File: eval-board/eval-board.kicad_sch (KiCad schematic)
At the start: 0 parts

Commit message: eval top level
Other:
- added sheet Barometer (baro.kicad_sch)
- added sheet FCU (fcu.kicad_sch)
- added sheet IMU0 (imu0.kicad_sch)
- added sheet IMU1 (imu1.kicad_sch)
- added sheet Magnetometer (mag.kicad_sch)
- added sheet PMU (pmu.kicad_sch)
- added sheet WCU (wcu.kicad_sch)

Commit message: pmu schematic
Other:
- sheet PMU ports: added +3V3A, +3V3D, +3V3D_PG, +5V, VIN; removed none
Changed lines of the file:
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@@
 	)
 	(sheet
-		(at 30.48 88.9)
-		(size 40.64 38.1)
+		(at 35.56 92.71)
+		(size 17.78 12.7)
 		(exclude_from_sim no)
 		(in_bom yes)
@@
 		)
 		(property "Sheetname" "PMU"
-			(at 30.48 88.1884 0)
+			(at 35.56 91.9984 0)
 			(show_name no)
 			(do_not_autoplace no)
@@
 		)
 		(property "Sheetfile" "pmu.kicad_sch"
-			(at 30.48 127.5846 0)
+			(at 35.56 105.9946 0)
 			(show_name no)
 			(do_not_autoplace no)
@@
 			)
 		)
+		(pin "VIN" input
+			(at 35.56 95.25 180)
+			(effects
+				(font
+					(size 1.27 1.27)
+				)
+				(justify left)
+			)
+		)
+		(pin "+5V" output
+			(at 53.34 95.25 0)
+			(effects
+				(font
+					(size 1.27 1.27)
+				)
+				(justify right)
+			)
+		)
+		(pin "+3V3A" output
+			(at 53.34 97.79 0)
+			(effects
+				(font
+					(size 1.27 1.27)
+				)
+				(justify right)
+			)
+		)
+		(pin "+3V3D_PG" output
+			(at 53.34 102.87 0)
+			(effects
+				(font
+					(size 1.27 1.27)
+				)
+				(justify right)
+			)
+		)
+		(pin "+3V3D" output
+			(at 53.34 100.33 0)
+			(effects
+				(font
+					(size 1.27 1.27)
+				)
+				(justify right)
+			)
+		)

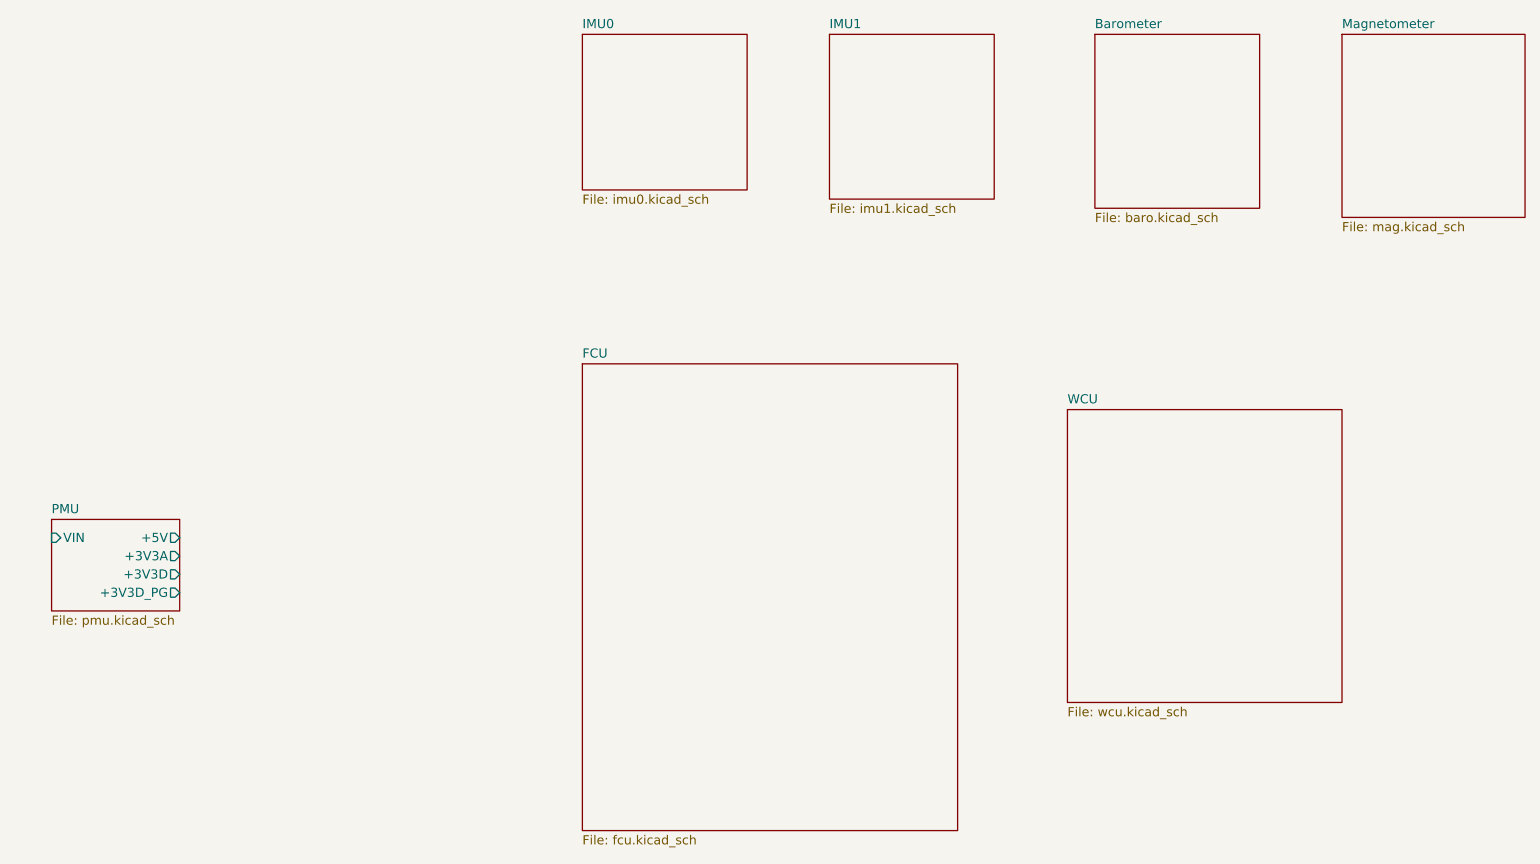
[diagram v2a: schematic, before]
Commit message: imu0 - lsm6dso
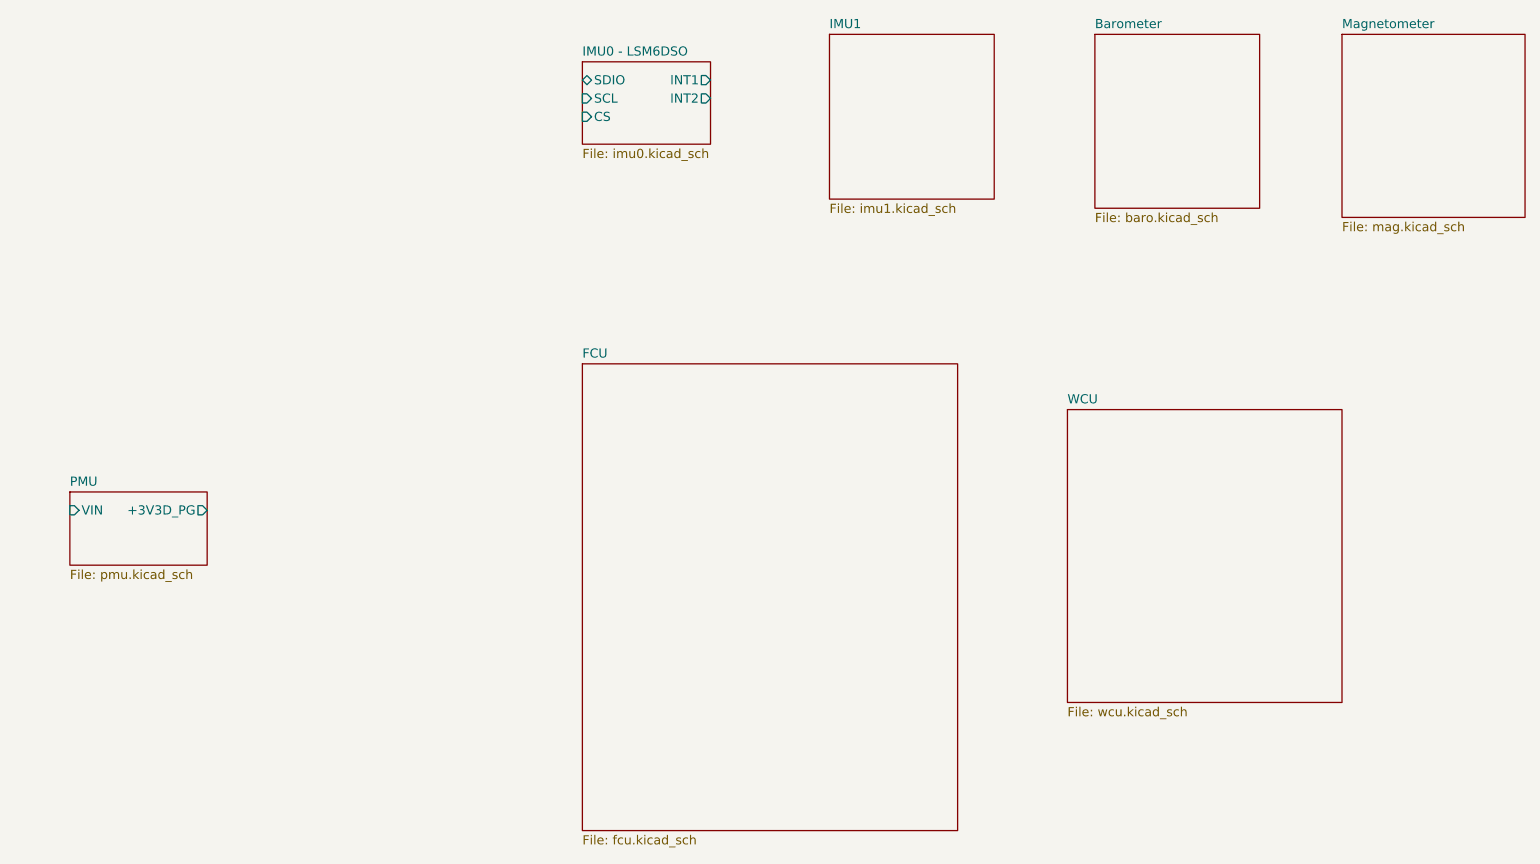
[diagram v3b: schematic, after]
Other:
- sheet IMU0 renamed IMU0 - LSM6DSO
- sheet IMU0 - LSM6DSO ports: added CS, INT1, INT2, SCL, SDIO; removed none
- sheet PMU ports: added none; removed +3V3A, +3V3D, +5V
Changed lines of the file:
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@@
 	)
 	(sheet
-		(at 109.22 25.4)
-		(size 22.86 21.59)
+		(at 109.22 29.21)
+		(size 17.78 11.43)
 		(exclude_from_sim no)
 		(in_bom yes)
@@
 			(color 0 0 0 0)
 		)
-		(property "Sheetname" "IMU0"
-			(at 109.22 24.6884 0)
+		(property "Sheetname" "IMU0 - LSM6DSO"
+			(at 109.22 28.4984 0)
 			(show_name no)
 			(do_not_autoplace no)
@@
 		)
 		(property "Sheetfile" "imu0.kicad_sch"
-			(at 109.22 47.5746 0)
+			(at 109.22 41.2246 0)
 			(show_name no)
 			(do_not_autoplace no)
@@
 				)
 				(justify left top)
+			)
+		)
+		(pin "SDIO" bidirectional
+			(at 109.22 31.75 180)
+			(effects
+				(font
+					(size 1.27 1.27)
+				)
+				(justify left)
+			)
+		)
+		(pin "SCL" input
+			(at 109.22 34.29 180)
+			(effects
+				(font
+					(size 1.27 1.27)
+				)
+				(justify left)
+			)
+		)
+		(pin "CS" input
+			(at 109.22 36.83 180)
+			(effects
+				(font
+					(size 1.27 1.27)
+				)
+				(justify left)
+			)
+		)
+		(pin "INT2" output
+			(at 127 34.29 0)
+			(effects
+				(font
+					(size 1.27 1.27)
+				)
+				(justify right)
+			)
+		)
+		(pin "INT1" output
+			(at 127 31.75 0)
+			(effects
+				(font
+					(size 1.27 1.27)
+				)
+				(justify right)
 			)
 		)
@@
 	)
 	(sheet
-		(at 35.56 92.71)
-		(size 17.78 12.7)
+		(at 38.1 88.9)
+		(size 19.05 10.16)
 		(exclude_from_sim no)
 		(in_bom yes)
@@
 		)
 		(property "Sheetname" "PMU"
-			(at 35.56 91.9984 0)
+			(at 38.1 88.1884 0)
 			(show_name no)
 			(do_not_autoplace no)
@@
 		)
 		(property "Sheetfile" "pmu.kicad_sch"
-			(at 35.56 105.9946 0)
+			(at 38.1 99.6446 0)
 			(show_name no)
 			(do_not_autoplace no)
@@
 		)
 		(pin "VIN" input
-			(at 35.56 95.25 180)
+			(at 38.1 91.44 180)
 			(effects
 				(font
@@
 			)
 		)
-		(pin "+5V" output
-			(at 53.34 95.25 0)
+		(pin "+3V3D_PG" output
+			(at 57.15 91.44 0)
 			(effects
 				(font
-					(size 1.27 1.27)
-				)
-				(justify right)
-			)
-		)
-		(pin "+3V3A" output
-			(at 53.34 97.79 0)
-			(effects
-				(font
-					(size 1.27 1.27)
-				)
-				(justify right)
-			)
-		)
-		(pin "+3V3D_PG" output
-			(at 53.34 102.87 0)
-			(effects
-				(font
-					(size 1.27 1.27)
-				)
-				(justify right)
-			)
-		)
-		(pin "+3V3D" output
-			(at 53.34 100.33 0)
-			(effects
-				(font

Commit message: imu1, baro, mag
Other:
- sheet Barometer renamed Barometer - BMP388
- sheet IMU1 renamed IMU1 - BMI270
- sheet Barometer - BMP388 ports: added INT, SCL, SDA; removed none
- sheet IMU0 - LSM6DSO ports: added SCLK; removed SCL
- sheet IMU1 - BMI270 ports: added CS, INT1, INT2, SCLK, SDIO; removed none
- sheet Magnetometer ports: added SCL, SDA; removed none
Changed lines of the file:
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@@
 	(paper "A4")
 	(sheet
-		(at 143.51 25.4)
-		(size 22.86 22.86)
-		(exclude_from_sim no)
-		(in_bom yes)
-		(on_board yes)
-		(dnp no)
-		(fields_autoplaced yes)
-		(stroke
-			(width 0.1524)
-			(type solid)
-		)
-		(fill
-			(color 0 0 0 0)
-		)
-		(property "Sheetname" "IMU1"
-			(at 143.51 24.6884 0)
+		(at 69.85 38.1)
+		(size 20.32 11.43)
+		(exclude_from_sim no)
+		(in_bom yes)
+		(on_board yes)
+		(dnp no)
+		(fields_autoplaced yes)
+		(stroke
+			(width 0.1524)
+			(type solid)
+		)
+		(fill
+			(color 0 0 0 0)
+		)
+		(property "Sheetname" "IMU1 - BMI270"
+			(at 69.85 37.3884 0)
 			(show_name no)
 			(do_not_autoplace no)
@@
 		)
 		(property "Sheetfile" "imu1.kicad_sch"
-			(at 143.51 48.8446 0)
-			(show_name no)
-			(do_not_autoplace no)
-			(effects
-				(font
-					(size 1.27 1.27)
-				)
-				(justify left top)
+			(at 69.85 50.1146 0)
+			(show_name no)
+			(do_not_autoplace no)
+			(effects
+				(font
+					(size 1.27 1.27)
+				)
+				(justify left top)
+			)
+		)
+		(pin "INT1" output
+			(at 90.17 40.64 0)
+			(effects
+				(font
+					(size 1.27 1.27)
+				)
+				(justify right)
+			)
+		)
+		(pin "INT2" output
+			(at 90.17 43.18 0)
+			(effects
+				(font
+					(size 1.27 1.27)
+				)
+				(justify right)
+			)
+		)
+		(pin "SDIO" bidirectional
+			(at 69.85 40.64 180)
+			(effects
+				(font
+					(size 1.27 1.27)
+				)
+				(justify left)
+			)
+		)
+		(pin "CS" input
+			(at 69.85 45.72 180)
+			(effects
+				(font
+					(size 1.27 1.27)
+				)
+				(justify left)
+			)
+		)
+		(pin "SCLK" input
+			(at 69.85 43.18 180)
+			(effects
+				(font
+					(size 1.27 1.27)
+				)
+				(justify left)
 			)
 		)
@@
 	)
 	(sheet
-		(at 214.63 25.4)
-		(size 25.4 25.4)
+		(at 132.08 38.1)
+		(size 12.7 11.43)
 		(exclude_from_sim no)
 		(in_bom yes)
@@
 		)
 		(property "Sheetname" "Magnetometer"
-			(at 214.63 24.6884 0)
+			(at 132.08 37.3884 0)
 			(show_name no)
 			(do_not_autoplace no)
@@
 		)
 		(property "Sheetfile" "mag.kicad_sch"
-			(at 214.63 51.3846 0)
-			(show_name no)
-			(do_not_autoplace no)
-			(effects
-				(font
-					(size 1.27 1.27)
-				)
-				(justify left top)
+			(at 132.08 50.1146 0)
+			(show_name no)
+			(do_not_autoplace no)
+			(effects
+				(font
+					(size 1.27 1.27)
+				)
+				(justify left top)
+			)
+		)
+		(pin "SDA" bidirectional
+			(at 132.08 40.64 180)
+			(effects
+				(font
+					(size 1.27 1.27)
+				)
+				(justify left)
+			)
+		)
+		(pin "SCL" input
+			(at 132.08 43.18 180)
+			(effects
+				(font
+					(size 1.27 1.27)
+				)
+				(justify left)
 			)
 		)
@@
 	)
 	(sheet
-		(at 180.34 25.4)
-		(size 22.86 24.13)
-		(exclude_from_sim no)
-		(in_bom yes)
-		(on_board yes)
-		(dnp no)
-		(fields_autoplaced yes)
-		(stroke
-			(width 0.1524)
-			(type solid)
-		)
-		(fill
-			(color 0 0 0 0)
-		)
-		(property "Sheetname" "Barometer"
-			(at 180.34 24.6884 0)
+		(at 100.33 38.1)
+		(size 19.05 11.43)
+		(exclude_from_sim no)
+		(in_bom yes)
+		(on_board yes)
+		(dnp no)
+		(fields_autoplaced yes)
+		(stroke
+			(width 0.1524)
+			(type solid)
+		)
+		(fill
+			(color 0 0 0 0)
+		)
+		(property "Sheetname" "Barometer - BMP388"
+			(at 100.33 37.3884 0)
 			(show_name no)
 			(do_not_autoplace no)
@@
 		)
 		(property "Sheetfile" "baro.kicad_sch"
-			(at 180.34 50.1146 0)
-			(show_name no)
-			(do_not_autoplace no)
-			(effects
-				(font
-					(size 1.27 1.27)
-				)
-				(justify left top)
+			(at 100.33 50.1146 0)
+			(show_name no)
+			(do_not_autoplace no)
+			(effects
+				(font
+					(size 1.27 1.27)
+				)
+				(justify left top)
+			)
+		)
+		(pin "SDA" bidirectional
+			(at 100.33 40.64 180)
+			(effects
+				(font
+					(size 1.27 1.27)
+				)
+				(justify left)
+			)
+		)
+		(pin "INT" output
+			(at 119.38 40.64 0)
+			(effects
+				(font
+					(size 1.27 1.27)
+				)
+				(justify right)
+			)
+		)
+		(pin "SCL" input
+			(at 100.33 43.18 180)
+			(effects
+				(font
+					(size 1.27 1.27)
+				)
+				(justify left)
 			)
 		)
@@
 	)
 	(sheet
-		(at 109.22 29.21)
+		(at 41.91 38.1)
 		(size 17.78 11.43)
 		(exclude_from_sim no)
@@
 		)
 		(property "Sheetname" "IMU0 - LSM6DSO"
-			(at 109.22 28.4984 0)
+			(at 41.91 37.3884 0)
 			(show_name no)
 			(do_not_autoplace no)
@@
 		)
 		(property "Sheetfile" "imu0.kicad_sch"
-			(at 109.22 41.2246 0)
+			(at 41.91 50.1146 0)
 			(show_name no)
 			(do_not_autoplace no)
@@
 		)
 		(pin "SDIO" bidirectional
-			(at 109.22 31.75 180)
-			(effects
-				(font
-					(size 1.27 1.27)
-				)
-				(justify left)
-			)
-		)
-		(pin "SCL" input
-			(at 109.22 34.29 180)
+			(at 41.91 40.64 180)
 			(effects
 				(font
@@
 		)
 		(pin "CS" input
-			(at 109.22 36.83 180)
+			(at 41.91 45.72 180)
 			(effects
 				(font
@@
 		)
 		(pin "INT2" output
-			(at 127 34.29 0)
+			(at 59.69 43.18 0)
 			(effects
 				(font
@@
 		)
 		(pin "INT1" output
-			(at 127 31.75 0)
-			(effects
-				(font
-					(size 1.27 1.27)
-				)
-				(justify right)
+			(at 59.69 40.64 0)
+			(effects
+				(font
+					(size 1.27 1.27)
+				)
+				(justify right)
+			)
+		)
+		(pin "SCLK" input
+			(at 41.91 43.18 180)
+			(effects
+				(font
+					(size 1.27 1.27)
+				)
+				(justify left)
 			)
 		)
@@
 	)
 	(sheet
-		(at 38.1 88.9)
+		(at 43.18 67.31)
 		(size 19.05 10.16)
 		(exclude_from_sim no)
@@
 		)
 		(property "Sheetname" "PMU"
-			(at 38.1 88.1884 0)
+			(at 43.18 66.5984 0)
 			(show_name no)
 			(do_not_autoplace no)
@@
 		)
 		(property "Sheetfile" "pmu.kicad_sch"
-			(at 38.1 99.6446 0)
+			(at 43.18 78.0546 0)
 			(show_name no)
 			(do_not_autoplace no)
@@
 		)
 		(pin "VIN" input
-			(at 38.1 91.44 180)
+			(at 43.18 69.85 180)
 			(effects
 				(font
@@
 		)
 		(pin "+3V3D_PG" output
-			(at 57.15 91.44 0)
-			(effects
-				(font
+			(at 62.23 69.85 0)
+			(effects
+				(font
